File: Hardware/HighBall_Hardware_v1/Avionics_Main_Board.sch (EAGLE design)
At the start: 7 parts

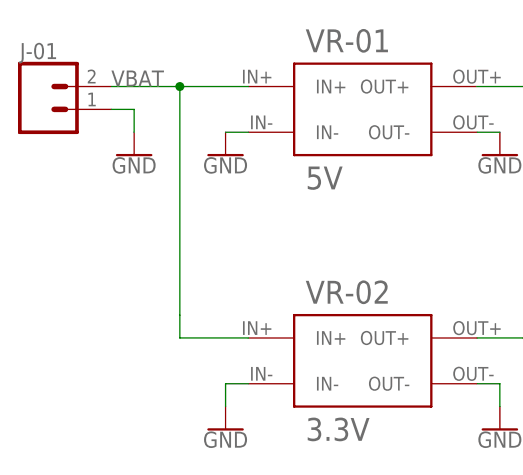
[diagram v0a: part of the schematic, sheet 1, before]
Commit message: Fixed battery connector
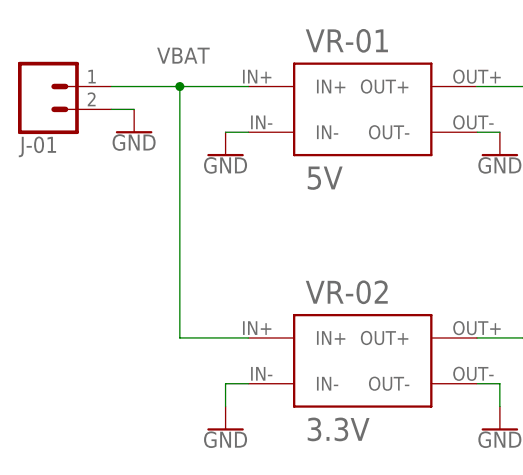
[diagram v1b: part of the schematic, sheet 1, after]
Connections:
- net GND: now also J-01.2; no longer J-01.1
- net VBAT: now also J-01.1; no longer J-01.2
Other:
- moved on the sheet: J-01
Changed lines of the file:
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@@
 <instance part="VR-01" gate="G$1" x="43.18" y="157.48"/>
 <instance part="VR-02" gate="G$1" x="43.18" y="129.54"/>
-<instance part="J-01" gate="G$1" x="15.24" y="162.56"/>
-<instance part="GND1" gate="1" x="25.4" y="157.48"/>
+<instance part="J-01" gate="G$1" x="15.24" y="165.1" rot="MR180"/>
+<instance part="GND1" gate="1" x="25.4" y="160.02"/>
 <instance part="GND2" gate="1" x="35.56" y="157.48"/>
 <instance part="GND3" gate="1" x="35.56" y="127"/>
@@
 <net name="VBAT" class="0">
 <segment>
-<pinref part="J-01" gate="G$1" pin="2"/>
 <pinref part="VR-01" gate="G$1" pin="IN+"/>
-<wire x1="22.86" y1="165.1" x2="30.48" y2="165.1" width="0.1524" layer="91"/>
 <wire x1="30.48" y1="165.1" x2="38.1" y2="165.1" width="0.1524" layer="91"/>
-<wire x1="30.48" y1="165.1" x2="30.48" y2="139.7" width="0.1524" layer="91"/>
-<junction x="30.48" y="165.1"/>
-<wire x1="30.48" y1="139.7" x2="30.48" y2="137.16" width="0.1524" layer="91"/>
+<wire x1="30.48" y1="165.1" x2="30.48" y2="137.16" width="0.1524" layer="91"/>
 <pinref part="VR-02" gate="G$1" pin="IN+"/>
 <wire x1="30.48" y1="137.16" x2="38.1" y2="137.16" width="0.1524" layer="91"/>
-<label x="22.86" y="165.1" size="1.778" layer="95"/>
+<label x="27.94" y="167.64" size="1.778" layer="95"/>
+<pinref part="J-01" gate="G$1" pin="1"/>
+<wire x1="22.86" y1="165.1" x2="30.48" y2="165.1" width="0.1524" layer="91"/>
+<junction x="30.48" y="165.1"/>
 </segment>
 </net>
 <net name="GND" class="0">
-<segment>
-<pinref part="J-01" gate="G$1" pin="1"/>
-<wire x1="22.86" y1="162.56" x2="25.4" y2="162.56" width="0.1524" layer="91"/>
-<wire x1="25.4" y1="162.56" x2="25.4" y2="160.02" width="0.1524" layer="91"/>
-<pinref part="GND1" gate="1" pin="GND"/>
-</segment>
 <segment>
 <pinref part="VR-01" gate="G$1" pin="IN-"/>
@@
 <wire x1="66.04" y1="132.08" x2="63.5" y2="132.08" width="0.1524" layer="91"/>
 </segment>
+<segment>
+<pinref part="J-01" gate="G$1" pin="2"/>
+<pinref part="GND1" gate="1" pin="GND"/>
+<wire x1="22.86" y1="162.56" x2="25.4" y2="162.56" width="0.1524" layer="91"/>
+</segment>
 </net>

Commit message: Avionics Schematic version A
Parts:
- removed B1: SPARKFUN_LOGIC_LEVEL_CONVERTERLOCK, SparkFun-Boards:SPARKFUN_LOGIC_LEVEL_CONVERTERLOCK
- removed B2: ARDUINO_MEGA_R3FULL, SparkFun-Boards:ARDUINO_MEGA_R3FULL
- removed TIT-02: LM335TO-92, High Ball Library:LM335TO-92
- removed U$2: RAZOR_IMU, High Ball Library:RAZOR_IMU
- added C-1: ARDUINO_MEGA_R3FULL, SparkFun-Boards:ARDUINO_MEGA_R3FULL
- added GPS-01: TITAN_X1_BREAKOUT, High Ball Library:TITAN_X1_BREAKOUT
- added HE-01, HE-02: (no value), SparkFun-Connectors:CONN_02LOCK
- added IMU-01: RAZOR_IMU, High Ball Library:RAZOR_IMU
- added LC-01: SPARKFUN_LOGIC_LEVEL_CONVERTERLOCK, SparkFun-Boards:SPARKFUN_LOGIC_LEVEL_CONVERTERLOCK
- added M-01, M-02: (no value), SparkFun-Connectors:CONN_03LOCK
- added PIT-01, PIT-02: MS5803-14BA_BREAKOUT, High Ball Library:MS5803-14BA_BREAKOUT
- added Q-01, Q-02: MOSFET-NCH-FQP30N06L, SparkFun-DiscreteSemi:MOSFET-NCH-FQP30N06L
- added TIT-01: LM335TO-92, High Ball Library:LM335TO-92
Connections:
- removed net AI-TIT-01: B2.A2, TIT-02.+
- new net GPS-01-INT: C-1.2, GPS-01.INT
- new net GPS-01-RESETN: GPS-01.RESETN, LC-01.LV_TXI_2
- new net GPS-01-RESETN_HV: C-1.23, LC-01.HV_TXO_2
- new net GPS-01-WAKE: GPS-01.WAKE, LC-01.LV_RXO_2
- new net GPS-01-WAKE_HV: C-1.22, LC-01.HV_RXI_2
- new net HE-01: C-1.4, Q-01.G
- new net HE-02: C-1.5, Q-02.G
- new net M-01: C-1.6, M-01.3
- new net M-02: C-1.7, M-02.3
- new net N$1: HE-01.2, Q-01.D
- new net N$2: HE-02.2, Q-02.D
- new net N$3: M-01.1
- new net N$4: M-01.2
- new net N$6: M-02.2
- new net N$7: M-02.1
- new net SCL: C-1.21(SCL), GPS-01.SCL, PIT-01.SCL/SCLK, PIT-02.SCL/SCLK
- new net SDA: C-1.20(SDA), GPS-01.SDA, PIT-01.SDA/SDI, PIT-02.SDA/SDI
- new net TIT-01: C-1.A2, TIT-01.+
- net AGND: now also C-1.GND@1, TIT-01.ADJ; no longer B2.GND@1, TIT-02.ADJ
- net GND: now also C-1.GND@0, GPS-01.GND, IMU-01.GND, LC-01.GND, LC-01.GND@2, PIT-01.GND, PIT-02.GND, Q-01.S, Q-02.S; no longer B1.GND, B1.GND@2, B2.GND@0, U$2.GND
- net IMU-01-RX: now also IMU-01.RX, LC-01.LV_TXI_1; no longer B1.LV_TXI_1, U$2.RX
- net IMU-01-RX_HV: now also C-1.16(TX2), LC-01.HV_TXO_1; no longer B1.HV_TXO_1, B2.16(TX2)
- net IMU-01-TX: now also IMU-01.TX, LC-01.LV_RXO_1; no longer B1.LV_RXO_1, U$2.TX
- net IMU-01-TX_HV: now also C-1.17(RX2), LC-01.HV_RXI_1; no longer B1.HV_RXI_1, B2.17(RX2)
- net VBAT: now also HE-01.1, HE-02.1
- net VCC_1: now also C-1.5V@0, IMU-01.VBAT, LC-01.HV, TIT-01.-; no longer B1.HV, B2.5V@0, TIT-02.-, U$2.VBAT
- net VCC_2: now also GPS-01.3V3, LC-01.LV, PIT-01.3V3, PIT-02.3V3; no longer B1.LV
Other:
- note added: "A"
- note added: "Altimeters"
- note added: "Ballast (M-01)"
- note added: "CONTROLLER AND I/O"
- note added: "Cut-Down (HE-02)"
- note added: "GPS Module"
- note added: "GPS-01"
- note added: "Gas Valve (M-02)"
- note added: "Heaters"
- note added: "I2C Address: 0x10"
- note added: "I2C Address: 0x76"
- note added: "I2C Address: 0x77"
- note added: "IMU-01"
- note added: "INSTRUMENTATION"
- note added: "Motors / Servos"
- note added: "PAYLOAD TEMPERATURE"
- note added: "PIT-01"
- note added: "PIT-02"
- note added: "POWER"
- note added: "Payload (HE-01)"
- note added: "RAZOR IMU"
- note added: "TIT-01"
- note added: "Voltage Regulators"

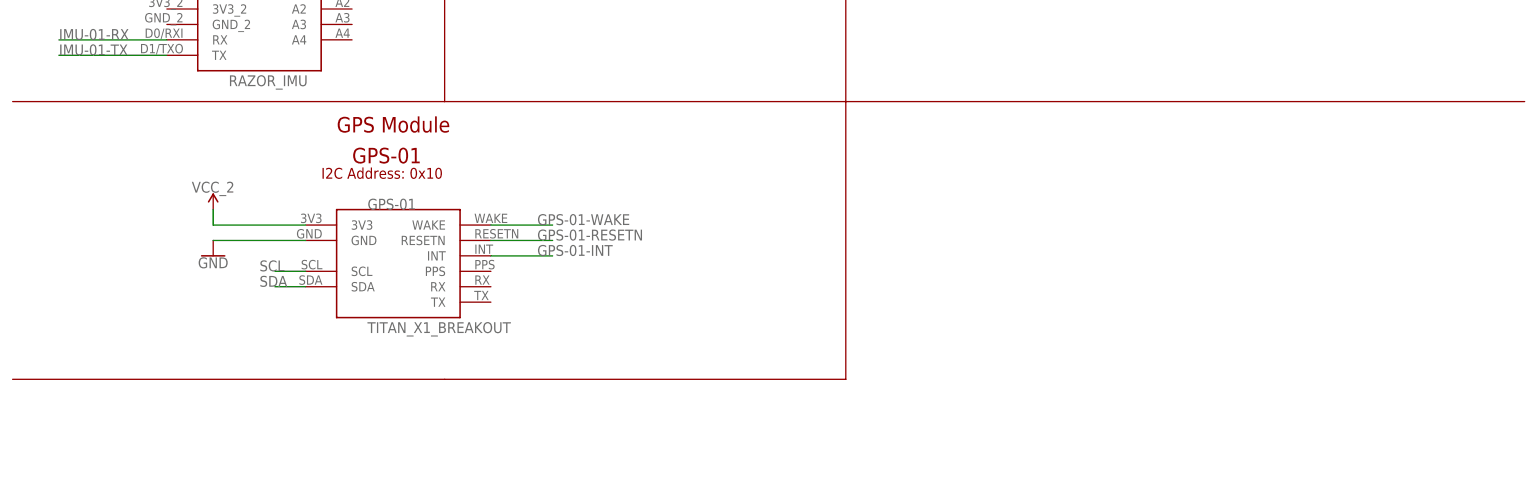
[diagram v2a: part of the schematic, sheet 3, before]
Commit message: Added RockBLOCK to schematic
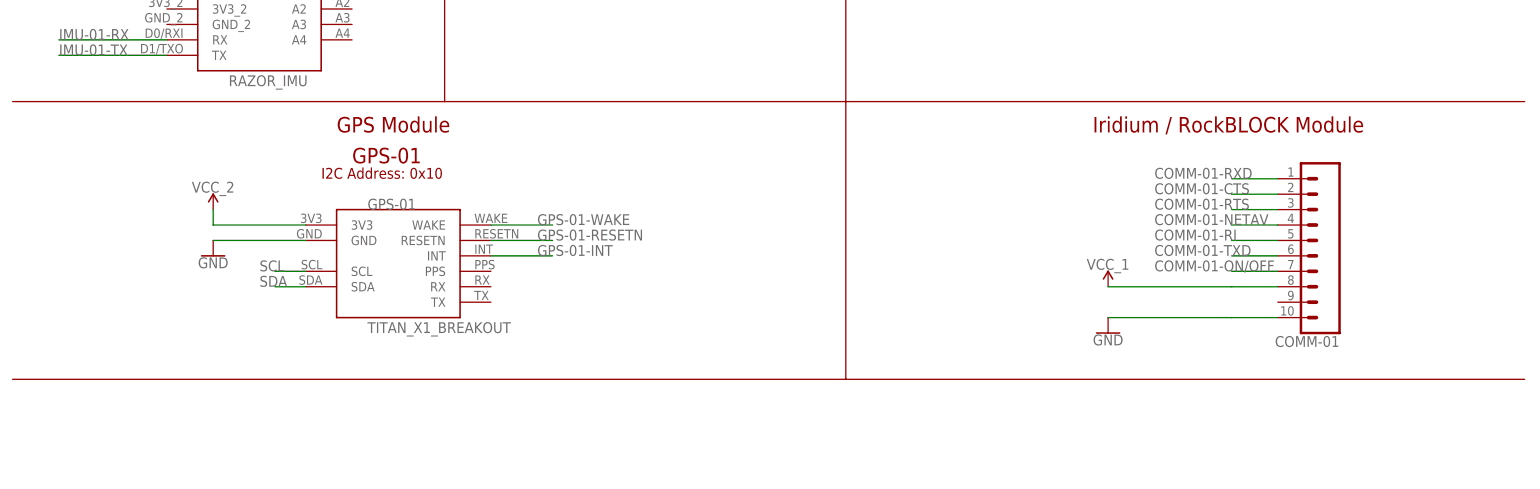
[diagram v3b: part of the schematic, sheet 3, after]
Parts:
- added COMM-01: (no value), SparkFun-Connectors:CONN_10"
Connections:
- new net COMM-01-CTS: COMM-01.2
- new net COMM-01-NETAV: C-1.24, COMM-01.4
- new net COMM-01-ON/OFF: C-1.25, COMM-01.7
- new net COMM-01-RI: C-1.3, COMM-01.5
- new net COMM-01-RTS: COMM-01.3
- new net COMM-01-RXD: C-1.19(RX1), COMM-01.1
- new net COMM-01-TXD: C-1.18(TX1), COMM-01.6
- net GND: now also COMM-01.10
- net VCC_1: now also COMM-01.8
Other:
- note added: "Iridium / RockBLOCK Module"
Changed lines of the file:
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@@
 <part name="SUPPLY12" library="SparkFun-PowerSymbols" library_urn="urn:adsk.eagle:library:530" deviceset="VCC_2" device=""/>
 <part name="GND16" library="SparkFun-PowerSymbols" library_urn="urn:adsk.eagle:library:530" deviceset="GND" device=""/>
+<part name="COMM-01" library="SparkFun-Connectors" library_urn="urn:adsk.eagle:library:513" deviceset="CONN_10" device="&quot;" package3d_urn="urn:adsk.eagle:package:38157/1"/>
+<part name="GND17" library="SparkFun-PowerSymbols" library_urn="urn:adsk.eagle:library:530" deviceset="GND" device=""/>
+<part name="SUPPLY13" library="SparkFun-PowerSymbols" library_urn="urn:adsk.eagle:library:530" deviceset="VCC_1" device=""/>
 </parts>
 <sheets>
@@
 <wire x1="160.02" y1="104.14" x2="154.94" y2="104.14" width="0.1524" layer="91"/>
 <label x="144.78" y="104.14" size="1.778" layer="95"/>
+</segment>
+</net>
+<net name="COMM-01-TXD" class="0">
+<segment>
+<pinref part="C-1" gate="G$1" pin="18(TX1)"/>
+<wire x1="195.58" y1="154.94" x2="200.66" y2="154.94" width="0.1524" layer="91"/>
+<label x="198.12" y="154.94" size="1.778" layer="95"/>
+</segment>
+</net>
+<net name="COMM-01-RXD" class="0">
+<segment>
+<pinref part="C-1" gate="G$1" pin="19(RX1)"/>
+<wire x1="195.58" y1="152.4" x2="200.66" y2="152.4" width="0.1524" layer="91"/>
+<label x="198.12" y="152.4" size="1.778" layer="95"/>
+</segment>
+</net>
+<net name="COMM-01-RI" class="0">
+<segment>
+<pinref part="C-1" gate="G$1" pin="3"/>
+<wire x1="160.02" y1="101.6" x2="154.94" y2="101.6" width="0.1524" layer="91"/>
+<label x="144.78" y="101.6" size="1.778" layer="95"/>
+</segment>
+</net>
+<net name="COMM-01-NETAV" class="0">
+<segment>
+<pinref part="C-1" gate="G$1" pin="24"/>
+<wire x1="195.58" y1="139.7" x2="200.66" y2="139.7" width="0.1524" layer="91"/>
+<label x="198.12" y="139.7" size="1.778" layer="95"/>
+</segment>
+</net>
+<net name="COMM-01-ON/OFF" class="0">
+<segment>
+<pinref part="C-1" gate="G$1" pin="25"/>
+<wire x1="195.58" y1="137.16" x2="200.66" y2="137.16" width="0.1524" layer="91"/>
+<label x="198.12" y="137.16" size="1.778" layer="95"/>
 </segment>
 </net>
@@
 <text x="55.88" y="114.3" size="2.54" layer="94">GPS-01</text>
 <text x="50.8" y="111.76" size="1.778" layer="94">I2C Address: 0x10</text>
-<wire x1="71.12" y1="78.74" x2="0" y2="78.74" width="0.1524" layer="94"/>
+<wire x1="137.16" y1="78.74" x2="0" y2="78.74" width="0.1524" layer="94"/>
 <wire x1="137.16" y1="124.46" x2="137.16" y2="78.74" width="0.1524" layer="94"/>
-<wire x1="137.16" y1="78.74" x2="71.12" y2="78.74" width="0.1524" layer="94"/>
 <text x="238.76" y="5.08" size="5.08" layer="94">A</text>
 <text x="149.86" y="25.4" size="5.08" layer="94">INSTRUMENTATION</text>
+<text x="177.8" y="119.38" size="2.54" layer="94">Iridium / RockBLOCK Module</text>
+<wire x1="137.16" y1="78.74" x2="248.92" y2="78.74" width="0.1524" layer="94"/>
 </plain>
 <instances>
@@
 <instance part="SUPPLY12" gate="G$1" x="33.02" y="106.68"/>
 <instance part="GND16" gate="1" x="33.02" y="99.06"/>
+<instance part="COMM-01" gate="G$1" x="218.44" y="93.98" rot="R180"/>
+<instance part="GND17" gate="1" x="180.34" y="86.36"/>
+<instance part="SUPPLY13" gate="G$2" x="180.34" y="93.98"/>
 </instances>
 <busses>
@@
 <pinref part="SUPPLY4" gate="G$2" pin="VCC_1"/>
 </segment>
+<segment>
+<pinref part="COMM-01" gate="G$1" pin="8"/>
+<wire x1="208.28" y1="93.98" x2="200.66" y2="93.98" width="0.1524" layer="91"/>
+<pinref part="SUPPLY13" gate="G$2" pin="VCC_1"/>
+<wire x1="200.66" y1="93.98" x2="180.34" y2="93.98" width="0.1524" layer="91"/>
+</segment>
 </net>
 <net name="AGND" class="0">
@@
 <pinref part="GND16" gate="1" pin="GND"/>
 </segment>
+<segment>
+<pinref part="COMM-01" gate="G$1" pin="10"/>
+<wire x1="208.28" y1="88.9" x2="200.66" y2="88.9" width="0.1524" layer="91"/>
+<pinref part="GND17" gate="1" pin="GND"/>
+<wire x1="200.66" y1="88.9" x2="180.34" y2="88.9" width="0.1524" layer="91"/>
+</segment>
 </net>
 <net name="VCC_2" class="0">
@@
 </segment>
 </net>
+<net name="COMM-01-RXD" class="0">
+<segment>
+<pinref part="COMM-01" gate="G$1" pin="1"/>
+<wire x1="208.28" y1="111.76" x2="200.66" y2="111.76" width="0.1524" layer="91"/>
+<label x="187.96" y="111.76" size="1.778" layer="95"/>
+</segment>
+</net>
+<net name="COMM-01-CTS" class="0">
+<segment>
+<pinref part="COMM-01" gate="G$1" pin="2"/>
+<wire x1="208.28" y1="109.22" x2="200.66" y2="109.22" width="0.1524" layer="91"/>
+<label x="187.96" y="109.22" size="1.778" layer="95"/>
+</segment>
+</net>
+<net name="COMM-01-RTS" class="0">
+<segment>
+<pinref part="COMM-01" gate="G$1" pin="3"/>
+<wire x1="208.28" y1="106.68" x2="200.66" y2="106.68" width="0.1524" layer="91"/>
+<label x="187.96" y="106.68" size="1.778" layer="95"/>
+</segment>
+</net>
+<net name="COMM-01-NETAV" class="0">
+<segment>
+<pinref part="COMM-01" gate="G$1" pin="4"/>
+<wire x1="208.28" y1="104.14" x2="200.66" y2="104.14" width="0.1524" layer="91"/>
+<label x="187.96" y="104.14" size="1.778" layer="95"/>
+</segment>
+</net>
+<net name="COMM-01-RI" class="0">
+<segment>
+<pinref part="COMM-01" gate="G$1" pin="5"/>
+<wire x1="208.28" y1="101.6" x2="200.66" y2="101.6" width="0.1524" layer="91"/>
+<label x="187.96" y="101.6" size="1.778" layer="95"/>
+</segment>
+</net>
+<net name="COMM-01-TXD" class="0">
+<segment>
+<pinref part="COMM-01" gate="G$1" pin="6"/>
+<wire x1="208.28" y1="99.06" x2="200.66" y2="99.06" width="0.1524" layer="91"/>
+<label x="187.96" y="99.06" size="1.778" layer="95"/>
+</segment>
+</net>
+<net name="COMM-01-ON/OFF" class="0">
+<segment>
+<pinref part="COMM-01" gate="G$1" pin="7"/>
+<wire x1="208.28" y1="96.52" x2="200.66" y2="96.52" width="0.1524" layer="91"/>
+<label x="187.96" y="96.52" size="1.778" layer="95"/>
+</segment>
+</net>
